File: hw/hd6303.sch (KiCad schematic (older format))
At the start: 13 parts, among them SW1 SW_Push, U1 XTAL_OSC_HALF_CAN, U2 MAX708, U3 HD6303RP, U4 74HCT02, U5 74HCT32, U6 27C512, U7 HM62256BLP-7, U8 74HCT138, U9 74LS374

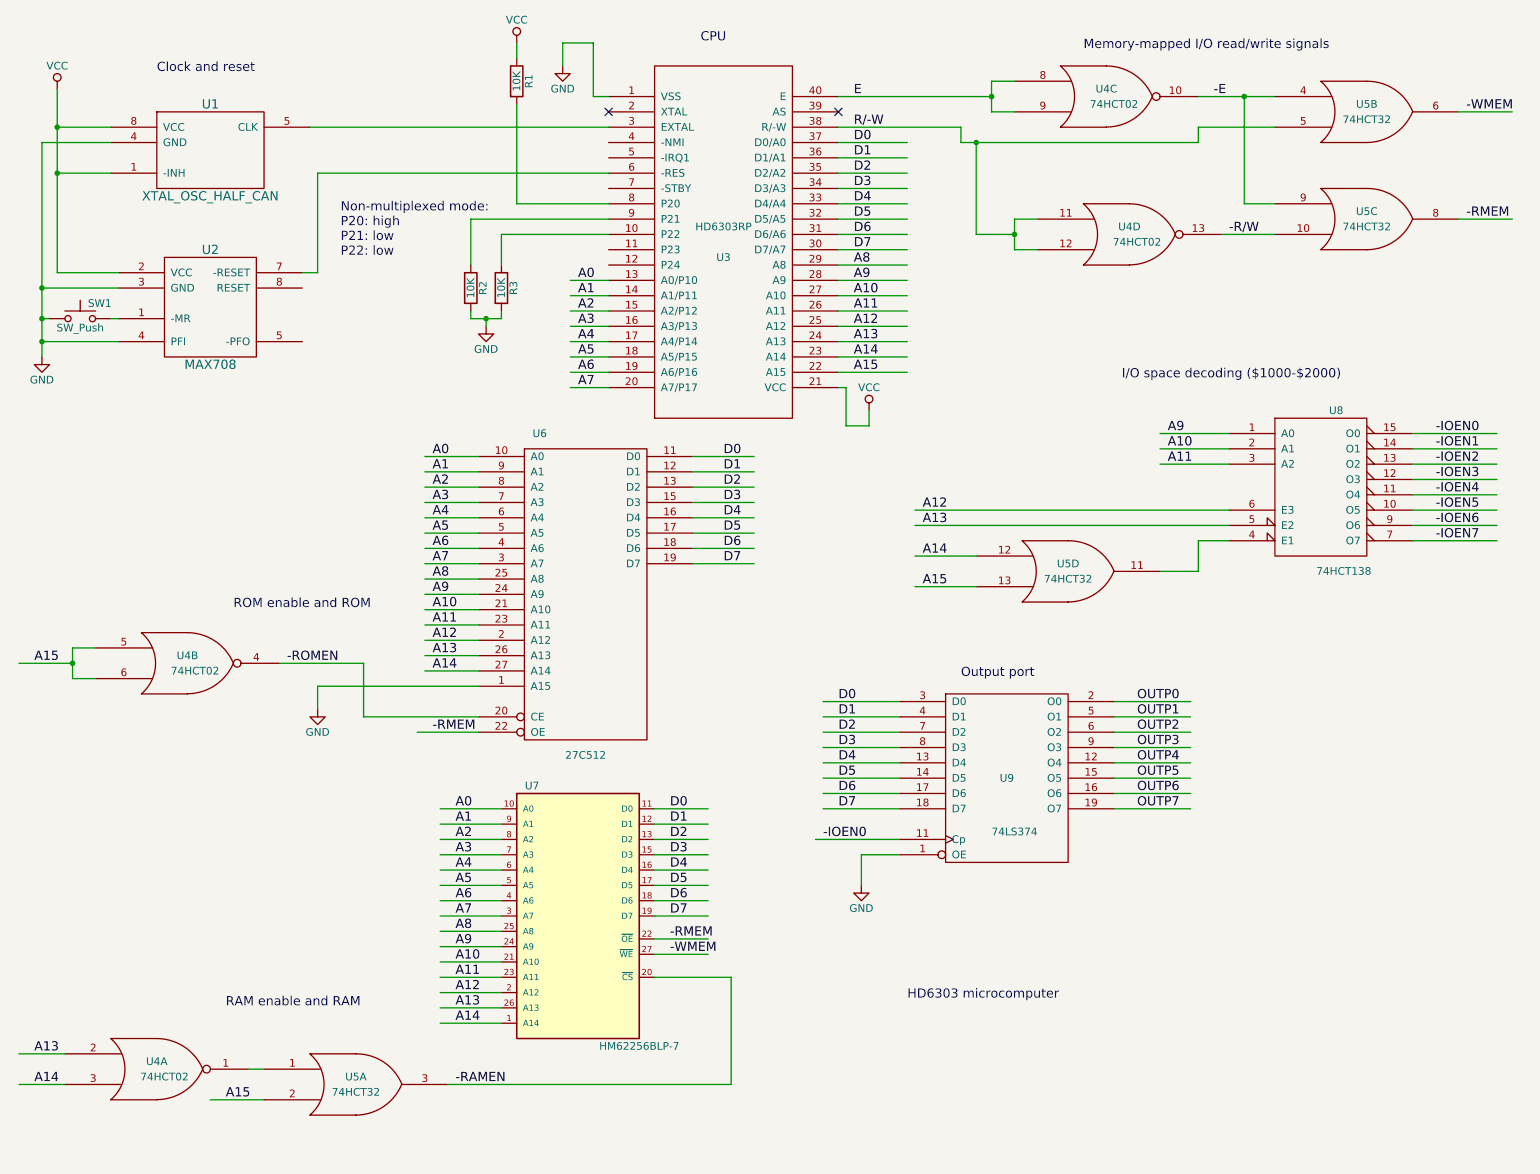
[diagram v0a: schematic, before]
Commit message: add pull-ups for -NMI, -IRQ1, -STBY
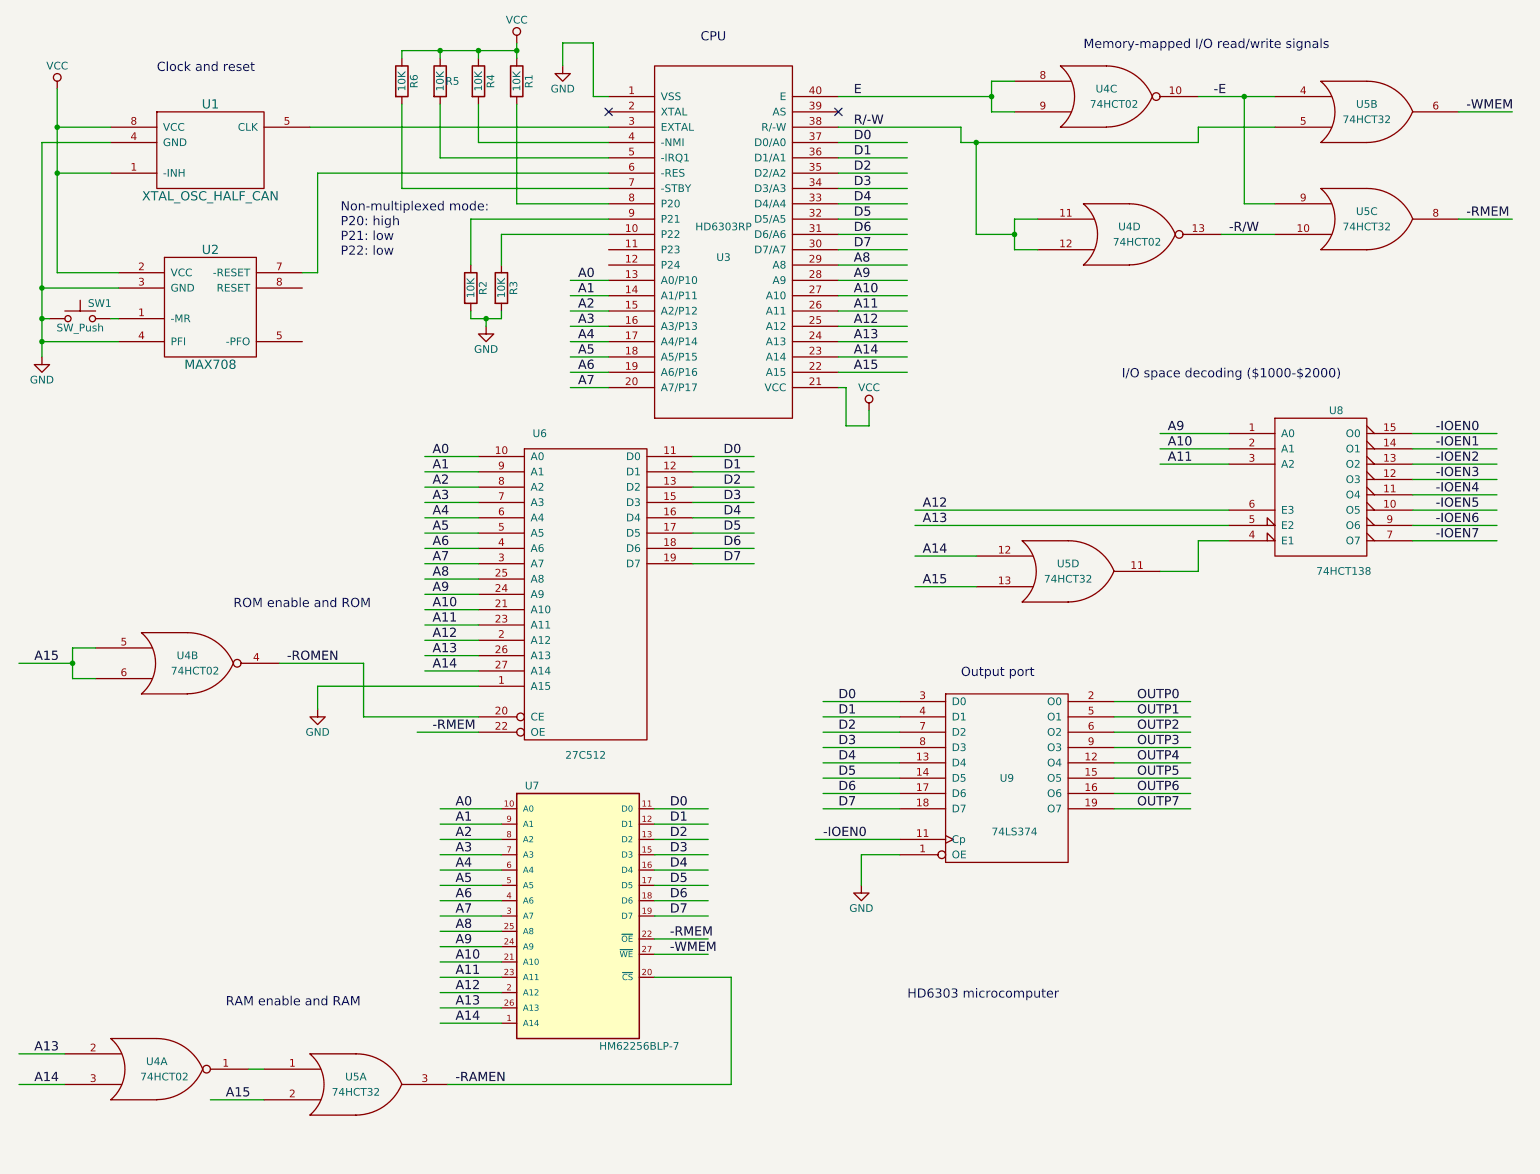
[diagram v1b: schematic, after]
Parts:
- added R4, R5, R6: 10K, symbol R
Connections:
- wire segments 190 -> 189
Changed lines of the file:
@@
 	1250 1250 900  1250
 Wire Wire Line
-	900  1000 900  1250
-Wire Wire Line
-	900  1250 900  1550
-Wire Wire Line
-	900  1550 900  2200
+	900  1000 900  2200
 Wire Wire Line
 	1250 1350 800  1350
 Wire Wire Line
-	800  1350 800  2300
-Wire Wire Line
-	800  2300 800  2500
-Wire Wire Line
-	800  2500 800  2650
-Wire Wire Line
-	800  2650 800  2750
+	800  1350 800  2750
 Wire Wire Line
 	4500 1050 4400 1050
@@
 	3800 2500 3800 2450
 Wire Wire Line
-	3600 2500 3700 2500
-Wire Wire Line
-	3700 2500 3800 2500
+	3600 2500 3800 2500
 Wire Wire Line
 	3700 2500 3700 2550
@@
 	1150 4650 1000 4650
 Wire Wire Line
-	1000 4650 1000 4750
-Wire Wire Line
-	1000 4750 1000 4850
+	1000 4650 1000 4850
 Wire Wire Line
 	1000 4750 650  4750
@@
 	3650 4800 3300 4800
 Wire Wire Line
-	8350 1050 8650 1050
-Wire Wire Line
-	8650 1050 8850 1050
+	8350 1050 8850 1050
 Wire Wire Line
 	7150 950  7000 950
 Wire Wire Line
-	7000 950  7000 1050
-Wire Wire Line
-	7000 1050 7000 1150
+	7000 950  7000 1150
 Wire Wire Line
 	6000 1050 7000 1050
@@
 	8350 1250 8350 1350
 Wire Wire Line
-	8350 1350 6900 1350
-Wire Wire Line
-	6900 1350 6800 1350
+	8350 1350 6800 1350
 Wire Wire Line
 	6000 1250 6800 1250
@@
 	7300 1850 7150 1850
 Wire Wire Line
-	7150 1850 7150 1950
-Wire Wire Line
-	7150 1950 7150 2050
+	7150 1850 7150 2050
 Wire Wire Line
 	7150 1950 6900 1950
@@
 Text Notes 6450 6950 0    60   ~ 0
 HD6303 microcomputer
+$Comp
+L R R4
+U 1 1 5A98743B
+P 3650 950
+F 0 "R4" V 3730 950 50  0000 C CNN
+F 1 "10K" V 3650 950 50  0000 C CNN
+F 2 "" V 3580 950 50  0001 C CNN
+F 3 "" H 3650 950 50  0001 C CNN
+	1    3650 950
+	1    0    0    -1
+$EndComp
+$Comp
+L R R5
+U 1 1 5A98748A
+P 3400 950
+F 0 "R5" H 3480 950 50  0000 C CNN
+F 1 "10K" V 3400 950 50  0000 C CNN
+F 2 "" V 3330 950 50  0001 C CNN
+F 3 "" H 3400 950 50  0001 C CNN
+	1    3400 950
+	1    0    0    -1
+$EndComp
+$Comp
+L R R6
+U 1 1 5A9874C9
+P 3150 950
+F 0 "R6" V 3230 950 50  0000 C CNN
+F 1 "10K" V 3150 950 50  0000 C CNN
+F 2 "" V 3080 950 50  0001 C CNN
+F 3 "" H 3150 950 50  0001 C CNN
+	1    3150 950
+	1    0    0    -1
+$EndComp
+Wire Wire Line
+	4500 1350 3650 1350
+Wire Wire Line
+	3650 1350 3650 1100
+Wire Wire Line
+	4500 1450 3400 1450
+Wire Wire Line
+	3400 1450 3400 1100
+Wire Wire Line
+	4500 1650 3150 1650
+Wire Wire Line
+	3150 1650 3150 1100
+Wire Wire Line
+	3650 800  3650 750
+Wire Wire Line
+	3150 750  3900 750
+Connection ~ 3900 750
+Wire Wire Line
+	3400 800  3400 750
+Connection ~ 3650 750
+Wire Wire Line
+	3150 800  3150 750
+Connection ~ 3400 750
 $EndSCHEMATC

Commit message: rearranged, better control for output port
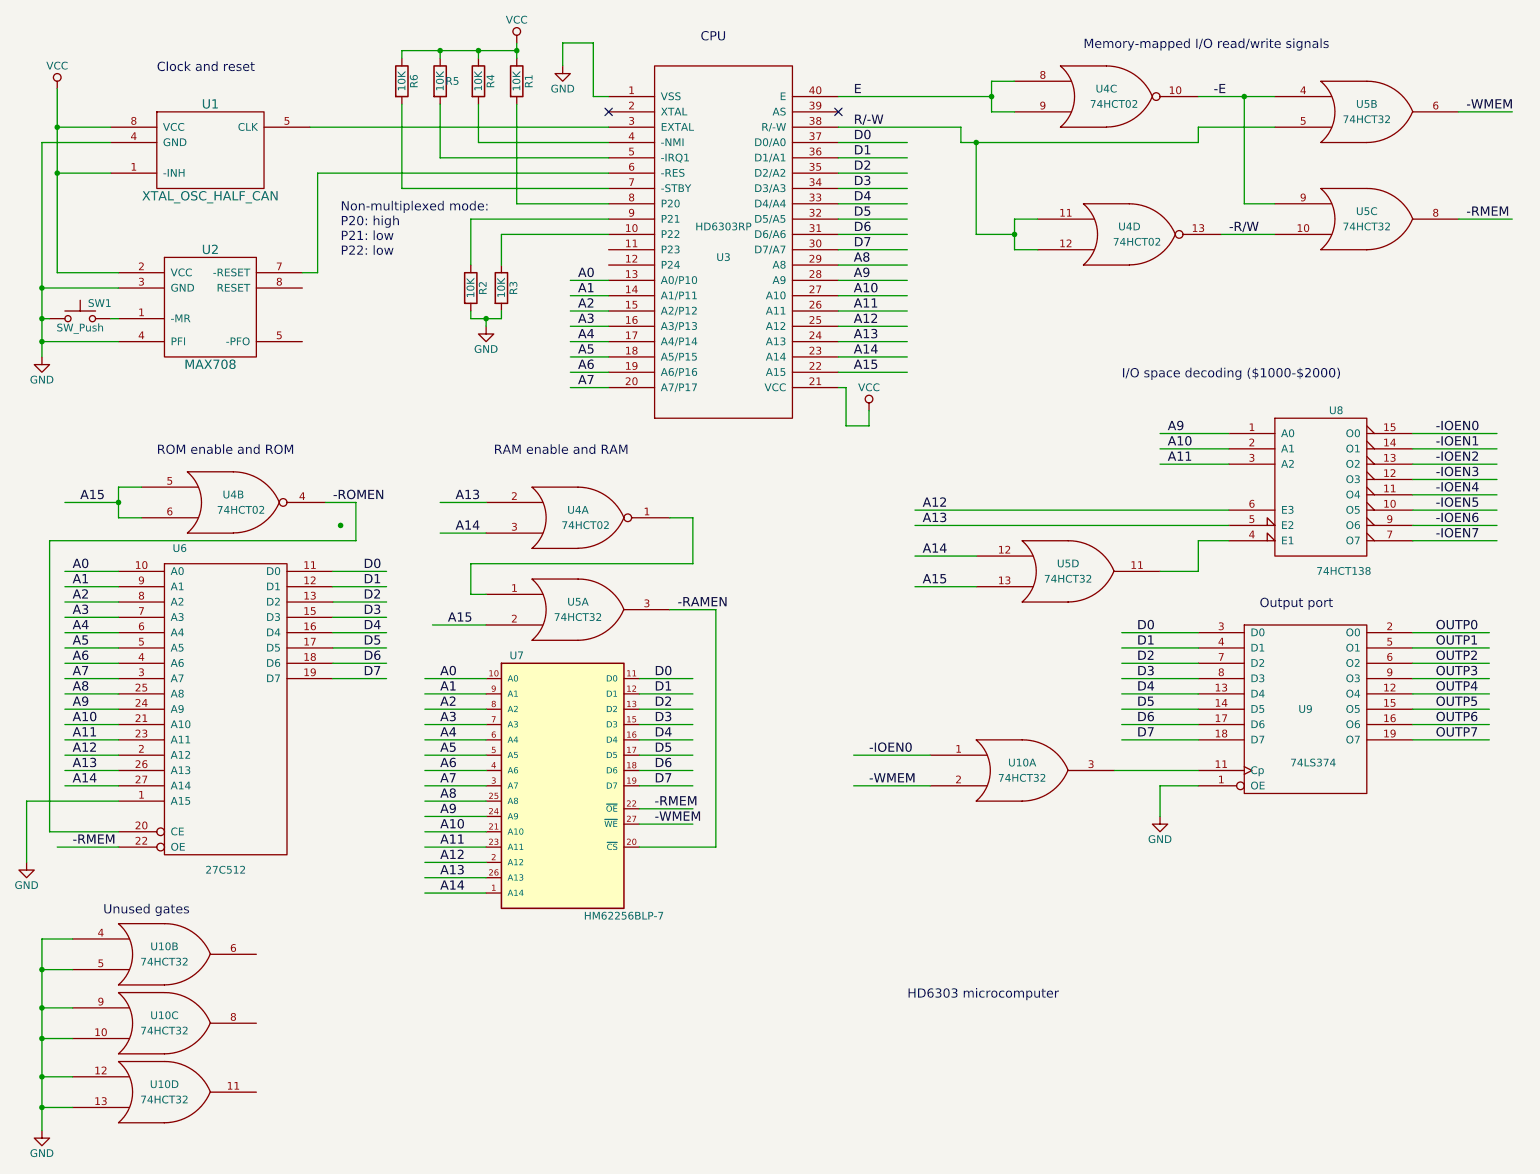
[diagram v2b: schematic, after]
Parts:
- added U10: 74HCT32, symbol 74LS32
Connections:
- wire segments 189 -> 204
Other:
- note added: "Unused gates"
- moved on the sheet: U4A, U4B, U5A, U6, U7, U9
